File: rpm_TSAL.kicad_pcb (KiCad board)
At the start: 2 copper layers, 0 parts

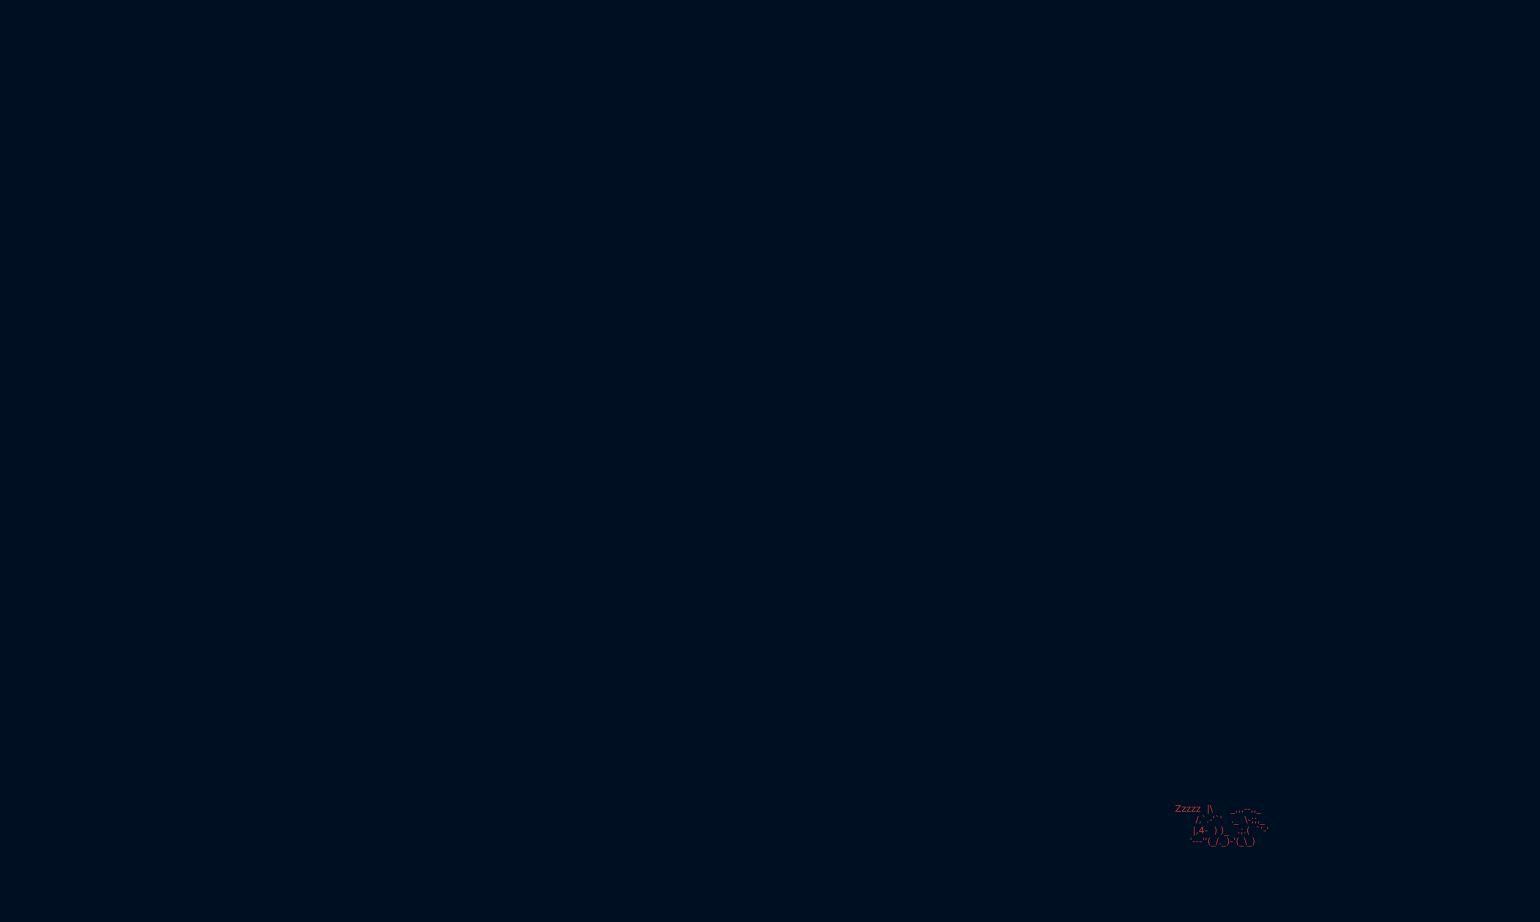
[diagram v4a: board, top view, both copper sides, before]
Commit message: TS Detection routing
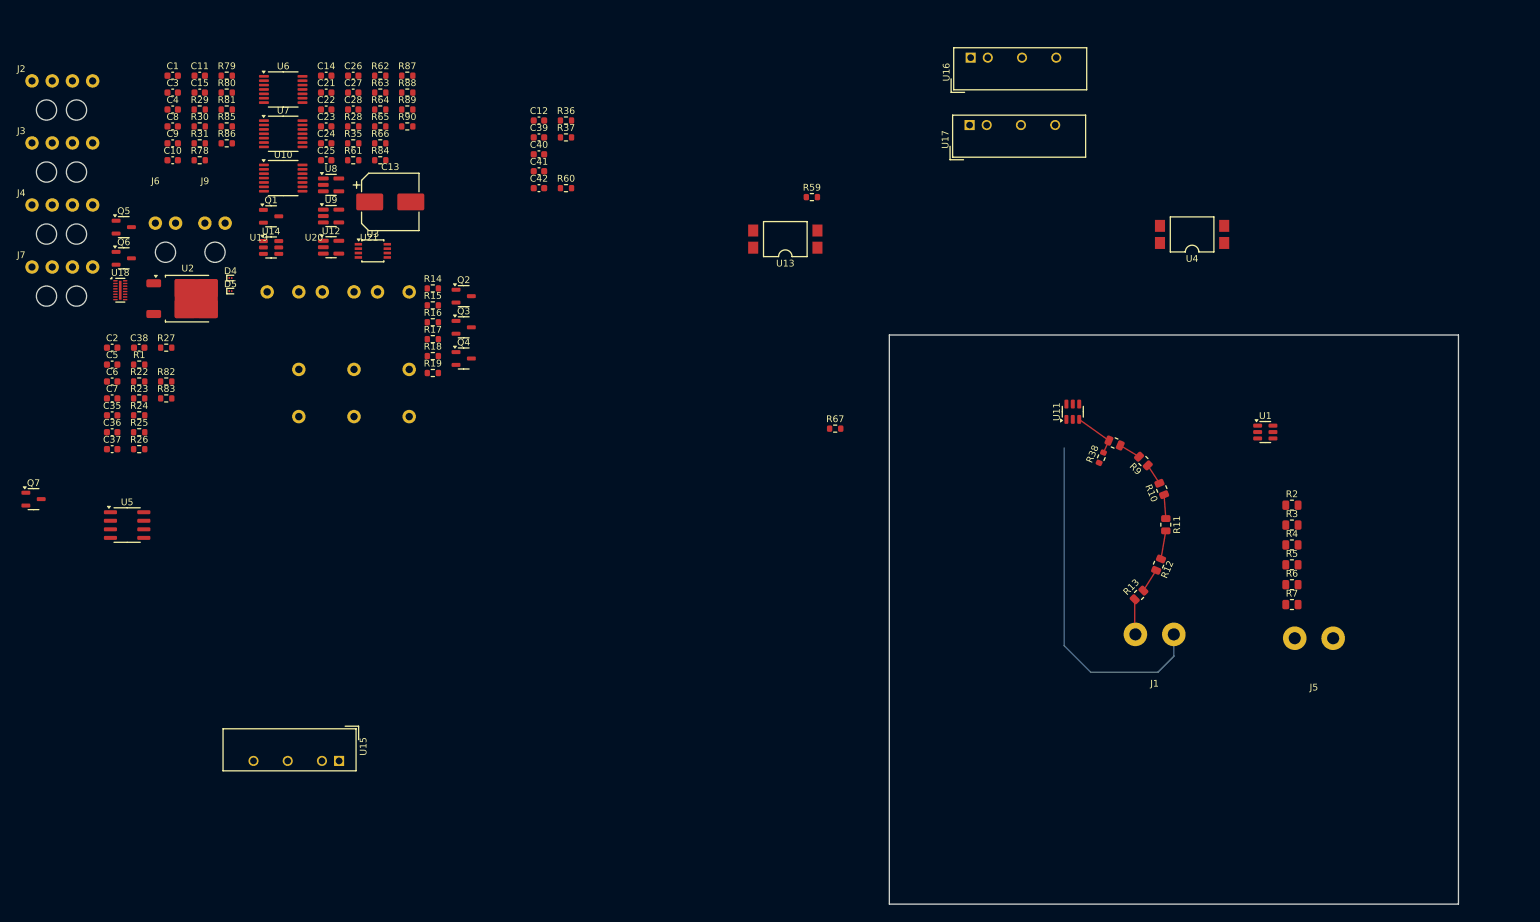
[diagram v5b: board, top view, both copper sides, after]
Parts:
- added C1: 100nF, Capacitor_SMD:C_0603_1608Metric, F.Cu at (45.5, 20.8)
- added C10: 100nF, Capacitor_SMD:C_0603_1608Metric, F.Cu at (45.5, 33.4)
- added C11: 10uF, Capacitor_SMD:C_0603_1608Metric, F.Cu at (49.5, 20.8)
- added C12: 100nF, Capacitor_SMD:C_0603_1608Metric, F.Cu at (99.9, 27.5)
- added C13: C_Polarized, Capacitor_SMD:CP_Elec_8x5.4, F.Cu at (77.8, 39.5)
- added C14: C, Capacitor_SMD:C_0603_1608Metric, F.Cu at (68.3, 20.8)
- added C15: 10uF, Capacitor_SMD:C_0603_1608Metric, F.Cu at (49.5, 23.3)
- added C2: 100nF, Capacitor_SMD:C_0603_1608Metric, F.Cu at (36.5, 61.2)
- added C21: 100nF, Capacitor_SMD:C_0603_1608Metric, F.Cu at (68.3, 23.3)
- added C22: 100nF, Capacitor_SMD:C_0603_1608Metric, F.Cu at (68.3, 25.8)
- added C23: 100nF, Capacitor_SMD:C_0603_1608Metric, F.Cu at (68.3, 28.4)
- added C24: 100nF, Capacitor_SMD:C_0603_1608Metric, F.Cu at (68.3, 30.9)
- added C25: 100nF, Capacitor_SMD:C_0603_1608Metric, F.Cu at (68.3, 33.4)
- added C26: 100nF, Capacitor_SMD:C_0603_1608Metric, F.Cu at (72.3, 20.8)
- added C27: 100nF, Capacitor_SMD:C_0603_1608Metric, F.Cu at (72.3, 23.3)
- added C28: 100nF, Capacitor_SMD:C_0603_1608Metric, F.Cu at (72.3, 25.8)
- added C3: 10uF, Capacitor_SMD:C_0603_1608Metric, F.Cu at (45.5, 23.3)
- added C35: 10uF, Capacitor_SMD:C_0603_1608Metric, F.Cu at (36.5, 71.2)
- added C36: 100nF, Capacitor_SMD:C_0603_1608Metric, F.Cu at (36.5, 73.7)
- added C37: 10uF, Capacitor_SMD:C_0603_1608Metric, F.Cu at (36.5, 76.2)
- added C38: 100nF, Capacitor_SMD:C_0603_1608Metric, F.Cu at (40.5, 61.2)
- added C39: 100nF, Capacitor_SMD:C_0603_1608Metric, F.Cu at (99.9, 30.0)
- added C4: 10uF, Capacitor_SMD:C_0603_1608Metric, F.Cu at (45.5, 25.8)
- added C40: 10uF, Capacitor_SMD:C_0603_1608Metric, F.Cu at (99.9, 32.5)
- added C41: 100nF, Capacitor_SMD:C_0603_1608Metric, F.Cu at (99.9, 35.0)
- added C42: 10uF, Capacitor_SMD:C_0603_1608Metric, F.Cu at (99.9, 37.5)
- added C5: 100nF, Capacitor_SMD:C_0603_1608Metric, F.Cu at (36.5, 63.7)
- added C6: 100nF, Capacitor_SMD:C_0603_1608Metric, F.Cu at (36.5, 66.2)
- added C7: 100nF, Capacitor_SMD:C_0603_1608Metric, F.Cu at (36.5, 68.7)
- added C8: 100nF, Capacitor_SMD:C_0603_1608Metric, F.Cu at (45.5, 28.4)
- added C9: 100nF, Capacitor_SMD:C_0603_1608Metric, F.Cu at (45.5, 30.9)
- added D4: ESD, Diode_SMD:Infineon_SG-WLL-2-3_0.58x0.28_P0.36mm, F.Cu at (54.1, 50.8)
- added D5: ESD, Diode_SMD:Infineon_SG-WLL-2-3_0.58x0.28_P0.36mm, F.Cu at (54.1, 52.8)
- added J1: Conn_01x02, wuerth_conn:657002130101, F.Cu at (188.4, 103.7)
- added J2: Conn_01x04, wuerth_conn:66200411022, F.Cu at (23.0, 20.3)
- added J3: Conn_01x04, wuerth_conn:66200411022, F.Cu at (23.0, 29.5)
- added J4: Conn_01x04, wuerth_conn:66200411022, F.Cu at (23.0, 38.7)
- added J5: Conn_01x02, wuerth_conn:657002130101, F.Cu at (212.0, 104.3)
- added J6: Conn_01x02, wuerth_conn:66200211024, F.Cu at (42.9, 42.7)
- added J7: Conn_01x04, wuerth_conn:66200411022, F.Cu at (23.0, 47.9)
- added J9: Conn_01x02, wuerth_conn:66200211024, F.Cu at (50.3, 42.7)
- added Q1: NMOS, Package_TO_SOT_SMD:SOT-23-3, F.Cu at (60.1, 41.7)
- added Q2: NMOS, Package_TO_SOT_SMD:SOT-23-3, F.Cu at (88.7, 53.5)
- added Q3: NMOS, Package_TO_SOT_SMD:SOT-23-3, F.Cu at (88.7, 58.2)
- added Q4: NMOS, Package_TO_SOT_SMD:SOT-23-3, F.Cu at (88.7, 62.8)
- added Q5: PMOS, Package_TO_SOT_SMD:SOT-23-3, F.Cu at (38.2, 43.3)
- added Q6: PMOS, Package_TO_SOT_SMD:SOT-23-3, F.Cu at (38.2, 47.9)
- added Q7: NMOS, Package_TO_SOT_SMD:SOT-23-3, F.Cu at (24.9, 83.7)
- added R1: 1k, Resistor_SMD:R_0603_1608Metric, F.Cu at (40.5, 63.7)
- added R10: 52k3, Resistor_SMD:R_0805_2012Metric, F.Cu at (192.3, 82.2)
- added R11: 52k3, Resistor_SMD:R_0805_2012Metric, F.Cu at (192.9, 87.5)
- added R12: 52k3, Resistor_SMD:R_0805_2012Metric, F.Cu at (191.8, 93.4)
- added R13: 52k3, Resistor_SMD:R_0805_2012Metric, F.Cu at (188.9, 97.9)
- added R14: 200R, Resistor_SMD:R_0603_1608Metric, F.Cu at (84.1, 52.4)
- added R15: 200R, Resistor_SMD:R_0603_1608Metric, F.Cu at (84.1, 54.9)
- added R16: 200R, Resistor_SMD:R_0603_1608Metric, F.Cu at (84.1, 57.4)
- added R17: 10k, Resistor_SMD:R_0603_1608Metric, F.Cu at (84.1, 59.9)
- added R18: 10k, Resistor_SMD:R_0603_1608Metric, F.Cu at (84.1, 62.4)
- added R19: 10k, Resistor_SMD:R_0603_1608Metric, F.Cu at (84.1, 64.9)
- added R2: 52k3, Resistor_SMD:R_0805_2012Metric, F.Cu at (211.6, 84.5)
- added R22: 1k, Resistor_SMD:R_0603_1608Metric, F.Cu at (40.5, 66.2)
- added R23: 1k, Resistor_SMD:R_0603_1608Metric, F.Cu at (40.5, 68.7)
- added R24: 12k, Resistor_SMD:R_0603_1608Metric, F.Cu at (40.5, 71.2)
- added R25: 1k, Resistor_SMD:R_0603_1608Metric, F.Cu at (40.5, 73.7)
- added R26: 1k, Resistor_SMD:R_0603_1608Metric, F.Cu at (40.5, 76.2)
- added R27: 10k, Resistor_SMD:R_0603_1608Metric, F.Cu at (44.5, 61.2)
- added R28: 30k, Resistor_SMD:R_0603_1608Metric, F.Cu at (72.3, 28.4)
- added R29: 10k, Resistor_SMD:R_0603_1608Metric, F.Cu at (49.5, 25.8)
- added R3: 52k3, Resistor_SMD:R_0805_2012Metric, F.Cu at (211.6, 87.5)
- added R30: 10k, Resistor_SMD:R_0603_1608Metric, F.Cu at (49.5, 28.4)
- added R31: 10k, Resistor_SMD:R_0603_1608Metric, F.Cu at (49.5, 30.9)
- added R35: 200R, Resistor_SMD:R_0603_1608Metric, F.Cu at (72.3, 30.9)
- added R36: 12k, Resistor_SMD:R_0603_1608Metric, F.Cu at (103.9, 27.5)
- added R37: 1k, Resistor_SMD:R_0603_1608Metric, F.Cu at (103.9, 30.0)
- added R38: 1k, Resistor_SMD:R_0603_1608Metric, F.Cu at (183.3, 77.5)
- added R4: 52k3, Resistor_SMD:R_0805_2012Metric, F.Cu at (211.6, 90.5)
- added R5: 52k3, Resistor_SMD:R_0805_2012Metric, F.Cu at (211.6, 93.4)
- added R59: 1k, Resistor_SMD:R_0603_1608Metric, F.Cu at (140.4, 38.8)
- added R6: 52k3, Resistor_SMD:R_0805_2012Metric, F.Cu at (211.6, 96.3)
- added R60: 1k, Resistor_SMD:R_0603_1608Metric, F.Cu at (103.9, 37.5)
- added R61: 10k, Resistor_SMD:R_0603_1608Metric, F.Cu at (72.3, 33.4)
- added R62: 10k, Resistor_SMD:R_0603_1608Metric, F.Cu at (76.3, 20.8)
- added R63: 33k, Resistor_SMD:R_0603_1608Metric, F.Cu at (76.3, 23.3)
- added R64: 33k, Resistor_SMD:R_0603_1608Metric, F.Cu at (76.3, 25.8)
- added R65: 10k, Resistor_SMD:R_0603_1608Metric, F.Cu at (76.3, 28.4)
- added R66: 10k, Resistor_SMD:R_0603_1608Metric, F.Cu at (76.3, 30.9)
- added R67: 1k, Resistor_SMD:R_0603_1608Metric, F.Cu at (143.8, 73.2)
- added R7: 52k3, Resistor_SMD:R_0805_2012Metric, F.Cu at (211.6, 99.3)
- added R78: 200R, Resistor_SMD:R_0603_1608Metric, F.Cu at (49.5, 33.4)
- added R79: 200R, Resistor_SMD:R_0603_1608Metric, F.Cu at (53.5, 20.8)
- added R8: 52k3, Resistor_SMD:R_0805_2012Metric, F.Cu at (185.3, 75.3)
- added R80: 10k, Resistor_SMD:R_0603_1608Metric, F.Cu at (53.5, 23.3)
- added R81: 10k, Resistor_SMD:R_0603_1608Metric, F.Cu at (53.5, 25.8)
- added R82: 200R, Resistor_SMD:R_0603_1608Metric, F.Cu at (44.5, 66.2)
- added R83: 10k, Resistor_SMD:R_0603_1608Metric, F.Cu at (44.5, 68.7)
- added R84: 30k, Resistor_SMD:R_0603_1608Metric, F.Cu at (76.3, 33.4)
- added R85: 30k, Resistor_SMD:R_0603_1608Metric, F.Cu at (53.5, 28.4)
- added R86: 7k5, Resistor_SMD:R_0603_1608Metric, F.Cu at (53.5, 30.9)
- added R87: 30k, Resistor_SMD:R_0603_1608Metric, F.Cu at (80.3, 20.8)
- added R88: 7k5, Resistor_SMD:R_0603_1608Metric, F.Cu at (80.3, 23.3)
- added R89: 7k5, Resistor_SMD:R_0603_1608Metric, F.Cu at (80.3, 25.8)
- added R9: 52k3, Resistor_SMD:R_0805_2012Metric, F.Cu at (189.6, 78.0)
- added R90: 7k5, Resistor_SMD:R_0603_1608Metric, F.Cu at (80.3, 28.4)
- added U1: OPA355NA, Package_TO_SOT_SMD:SOT-23-6, F.Cu at (207.6, 73.7)
- added U10: SN74HCS266PWR, Package_SO:TSSOP-14_4.4x5mm_P0.65mm, F.Cu at (61.9, 36.0)
- added U11: OPA355NA, Package_TO_SOT_SMD:SOT-23-6, F.Cu at (179.1, 70.7)
- added U12: 74LVC1G32GV, Package_SO:SC-74A-5_1.55x2.9mm_P0.95mm, F.Cu at (69.0, 46.3)
- added U13: SFH617A-1X007T, Package_DIP:SMDIP-4_W9.53mm_Clearance8mm, F.Cu at (136.4, 45.1)
- added U14: OPA355NA, Package_TO_SOT_SMD:SOT-23-6, F.Cu at (60.1, 46.3)
- added U15: TBA1-1211E, Converter_DCDC:Converter_DCDC_TRACO_TBA1-xxxxE_Single_THT, F.Cu at (70.2, 122.5)
- added U16: TBA1-0511E, Converter_DCDC:Converter_DCDC_TRACO_TBA1-xxxxE_Single_THT, F.Cu at (163.9, 18.1)
- added U17: TBA1-0511E, Converter_DCDC:Converter_DCDC_TRACO_TBA1-xxxxE_Single_THT, F.Cu at (163.8, 28.1)
- added U18: IP4252CZ16, Package_SON:Nexperia_HUSON-16_USON-16-1EP_1.35x3.3mm_P0.4mm_EP0.4x2.8mm, F.Cu at (37.7, 52.7)
- added U19: ~, Zettler:AZ9371, F.Cu at (58.3, 51.9)
- added U2: L7805, Package_TO_SOT_SMD:TO-252-2, F.Cu at (47.7, 53.9)
- added U20: ~, Zettler:AZ9371, F.Cu at (66.5, 51.9)
- added U21: ~, Zettler:AZ9371, F.Cu at (74.7, 51.9)
- added U3: 74LVC2G74, Package_SO:TSSOP-8_3x3mm_P0.65mm, F.Cu at (75.2, 46.8)
- added U4: SFH617A-1X007T, Package_DIP:SMDIP-4_W9.53mm_Clearance8mm, F.Cu at (196.8, 44.4)
- added U5: NE555D, Package_SO:SOIC-8_3.9x4.9mm_P1.27mm, F.Cu at (38.8, 87.5)
- added U6: CD74HC30PWR, Package_SO:TSSOP-14_4.4x5mm_P0.65mm, F.Cu at (61.9, 22.9)
- added U7: 4072, Package_SO:TSSOP-14_4.4x5mm_P0.65mm, F.Cu at (61.9, 29.4)
- added U8: 4001, Package_SO:SC-74A-5_1.55x2.9mm_P0.95mm, F.Cu at (69.0, 37.0)
- added U9: 74LVC1G32GV, Package_SO:SC-74A-5_1.55x2.9mm_P0.95mm, F.Cu at (69.0, 41.6)
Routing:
- net HV-: track 0.00 -> 51.5 mm
- net Net-(U11-+): track 0.00 -> 7.37 mm
- net  HV+: track 0.00 -> 5.25 mm
- net Net-(R11-Pad2): track 0.00 -> 4.23 mm
- net Net-(R12-Pad2): track 0.00 -> 3.56 mm
- net Net-(R10-Pad1): track 0.00 -> 3.55 mm
- net Net-(R8-Pad1): track 0.00 -> 3.25 mm
- net Net-(R10-Pad2): track 0.00 -> 3.18 mm
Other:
- board outline added: 84.5 x 84.5 mm
- board text removed: "Zzzzz |\ _,,,--,,_ /,`.-'`' ._ \-;;,_ |,4- ) )_ .;.( `'-' '---''(_/._)-'(_\_)"

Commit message: Misc.
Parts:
- moved U1 5.88 mm to (206.4, 68.0)
- moved U11 2.28 mm to (179.0, 73.0)
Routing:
- net Net-(U11-+): track 7.37 -> 6.50 mm
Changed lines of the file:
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@@
 		(tags "SMD DIP DIL PDIP SMDIP 2.54mm 9.53mm 375mil Clearance8mm")
 		(property "Reference" "U4"
-			(at 0 -3.6 360)
+			(at 0 -3.6 0)
 			(layer "F.SilkS")
 			(effects
@@
 		)
 		(property "Value" "SFH617A-1X007T"
-			(at -0.15 4.12 360)
+			(at -0.15 4.12 0)
 			(layer "F.Fab")
 			(effects
@@
 		)
 		(fp_text user "${REFERENCE}"
-			(at 0 0 360)
+			(at 0 0 0)
 			(layer "F.Fab")
 			(effects
@@
 		(tags "resistor")
 		(property "Reference" "R38"
-			(at 0 -1.43 67)
+			(at 0.030294 -1.808229 67)
 			(layer "F.SilkS")
 			(effects
@@
 	(footprint "Package_TO_SOT_SMD:SOT-23-6"
 		(layer "F.Cu")
-		(at 179.075 70.6875 90)
+		(at 179.025 72.9625 90)
 		(descr "SOT, 6 Pin (https://www.jedec.org/sites/default/files/docs/Mo-178c.PDF variant AB), generated with kicad-footprint-generator ipc_gullwing_generator.py")
 		(tags "SOT TO_SOT_SMD")
@@
 		(tags "SMD DIP DIL PDIP SMDIP 2.54mm 9.53mm 375mil Clearance8mm")
 		(property "Reference" "U13"
-			(at 0 -3.6 360)
+			(at 0 -3.6 0)
 			(layer "F.SilkS")
 			(effects
@@
 		)
 		(property "Value" "SFH617A-1X007T"
-			(at 0 3.6 360)
+			(at 0 3.6 0)
 			(layer "F.Fab")
 			(effects
@@
 		)
 		(fp_text user "${REFERENCE}"
-			(at 0 0 360)
+			(at 0 0 0)
 			(layer "F.Fab")
 			(effects
@@
 		(tags "resistor")
 		(property "Reference" "R8"
-			(at 0 -1.65 157)
+			(at 0.03661 1.749796 157)
 			(layer "F.SilkS")
-			(hide yes)
 			(effects
 				(font
@@
 	(footprint "Package_TO_SOT_SMD:SOT-23-6"
 		(layer "F.Cu")
-		(at 207.6375 73.7)
+		(at 206.3875 67.95)
 		(descr "SOT, 6 Pin (https://www.jedec.org/sites/default/files/docs/Mo-178c.PDF variant AB), generated with kicad-footprint-generator ipc_gullwing_generator.py")
 		(tags "SOT TO_SOT_SMD")
 		(property "Reference" "U1"
-			(at 0 -2.4 360)
+			(at 0 -2.4 0)
 			(layer "F.SilkS")
 			(effects
@@
 		)
 		(property "Value" "OPA355NA"
-			(at -0.55 2.4 360)
+			(at -0.55 2.4 0)
 			(layer "F.Fab")
 			(effects
@@
 		)
 		(fp_text user "${REFERENCE}"
-			(at 0 0 360)
+			(at 0 0 0)
 			(layer "F.Fab")
 			(effects
@@
 	)
 	(segment
-		(start 184.435039 74.968458)
-		(end 180.025 71.825)
+		(start 179.975 74.1)
+		(end 184.435039 74.968458)
 		(width 0.2)
 		(layer "F.Cu")

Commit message: TSAL Rev 0.2
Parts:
- removed J9: Conn_01x02, wuerth_conn:66200211024
- added J14: Conn_01x04, wuerth_conn:66200411022, F.Cu at (129.2, 103.0)
- R85: value 30k -> 30k
- R86, R88, R89, R90: value 7k5 -> e
- moved C5 168.5 mm to (205.0, 69.4), turned to -90 degrees
- moved R23 162.5 mm to (203.1, 72.2), turned to 90 degrees
- moved R24 160.7 mm to (201.2, 69.2), turned to 180 degrees
- moved R22 160.0 mm to (200.3, 75.7)
- moved C35 148.5 mm to (182.9, 46.1), turned to -90 degrees
- moved C36 147.3 mm to (181.2, 46.1), turned to -90 degrees
- moved R1 121.6 mm to (162.0, 57.6)
- moved C12 87.0 mm to (177.3, 67.0)
- moved R37 85.7 mm to (179.2, 70.9), turned to 90 degrees
- moved R36 84.2 mm to (176.7, 69.8), turned to 180 degrees
- moved R60 64.5 mm to (162.0, 65.5)
- moved R59 45.6 mm to (177.4, 65.5), turned to 180 degrees
- moved U13 37.9 mm to (167.4, 67.0)
- moved R67 36.6 mm to (177.0, 57.8), turned to 180 degrees
- moved U16 33.1 mm to (162.6, 51.2)
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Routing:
- net HV_RED-: track 0.00 -> 109.1 mm, vias 0 -> 3
- net +5V_{iso_RED}: track 0.00 -> 47.2 mm
- net Net-(U1-Pad1): track 0.00 -> 32.5 mm
- net +5V_{iso}: track 0.00 -> 22.4 mm, vias 0 -> 1
- net HV-: track 51.5 -> 66.6 mm, vias 0 -> 1
- net Net-(U11-Pad1): track 0.00 -> 6.96 mm
- net Net-(U1-+): track 0.00 -> 6.15 mm
- net  HV_RED+: track 0.00 -> 5.62 mm
- net Net-(R59-Pad2): track 0.00 -> 4.50 mm
- net Net-(U1--): track 0.00 -> 4.34 mm
- net Net-(R11-Pad2): track 4.23 -> 0.00 mm
- net Net-(R67-Pad2): track 0.00 -> 4.08 mm
- net Net-(R12-Pad2): track 3.56 -> 0.00 mm
- net Net-(R10-Pad1): track 3.55 -> 0.00 mm
- net Net-(U11--): track 0.00 -> 3.49 mm
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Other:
- board size 84.5 x 84.5 mm -> 71.6 x 69.5 mm
- copper layers 2 -> 4

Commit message: Added Seperate Project
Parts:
- removed D4: ESD, Diode_SMD:Infineon_SG-WLL-2-3_0.58x0.28_P0.36mm
- removed J5: Conn_01x02, wuerth_conn:657002130101
- removed Q6: PMOS, Package_TO_SOT_SMD:SOT-23-3
- removed R79: 200R, Resistor_SMD:R_0603_1608Metric
- removed R80: 10k, Resistor_SMD:R_0603_1608Metric
- added H1: MountingHole, MountingHole:MountingHole_3.2mm_M3_DIN965, F.Cu at (66.3, 21.2)
- added H2: MountingHole, MountingHole:MountingHole_3.2mm_M3_DIN965, F.Cu at (66.3, 28.3)
- added H3: MountingHole, MountingHole:MountingHole_3.2mm_M3_DIN965, F.Cu at (66.3, 35.5)
- added H4: MountingHole, MountingHole:MountingHole_3.2mm_M3_DIN965, F.Cu at (66.3, 42.6)
- J7: value Conn_01x04 -> Conn_01x02; footprint wuerth_conn:66200411022 -> wuerth_conn:66200211024
- moved R7 145.9 mm to (79.9, 33.8), turned to 0 degrees
- moved R6 143.9 mm to (79.9, 30.9), turned to 0 degrees
- moved R5 142.0 mm to (79.9, 27.9), turned to 0 degrees
- moved R4 140.0 mm to (79.9, 25.0), turned to 0 degrees
- moved R3 138.1 mm to (79.9, 22.0), turned to 0 degrees
- moved R2 136.1 mm to (79.9, 19.1), turned to 0 degrees
- moved U1 130.5 mm to (72.4, 46.0), turned to 0 degrees
- moved C5 130.1 mm to (84.1, 21.4), turned to 0 degrees
- moved R13 124.8 mm to (62.9, 96.4), turned to 0 degrees
- moved R23 123.7 mm to (88.1, 26.4), turned to 0 degrees
- moved R22 123.5 mm to (88.1, 23.9)
- moved R12 122.8 mm to (62.9, 93.5), turned to 0 degrees
- moved R11 120.8 mm to (62.9, 90.5), turned to 0 degrees
- moved R24 120.1 mm to (88.1, 28.9), turned to 0 degrees
- moved R10 118.8 mm to (62.9, 87.6), turned to 0 degrees
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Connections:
- net  HV+ renamed HV+
- net /LV Connectors/TSAL_LED_RED renamed /TSAL RED/TSAL_RED_OUT
- J7 pad 2: Net-(D4-A2) -> GND
- Q5 pad 1: +24V -> Net-(D5-A2)
- Q5 pad 3: Net-(D5-A2) -> +24V
- R7 pad 1:  HV_RED+ -> HV_RED+
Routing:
- net HV_RED-: track 109.1 -> 0.00 mm, vias 3 -> 0
- net HV-: track 66.6 -> 0.00 mm, vias 1 -> 0
- net +5V_{iso_RED}: track 47.2 -> 0.00 mm
- net Net-(U1-Pad1): track 32.5 -> 0.00 mm
- net +5V_{iso}: track 22.4 -> 0.00 mm, vias 1 -> 0
- net Net-(U11-Pad1): track 6.96 -> 0.00 mm
- net Net-(U1-+): track 6.15 -> 0.00 mm
- net  HV_RED+: track 5.62 -> 0.00 mm
- net HV+: track 5.40 -> 0.00 mm
- net Net-(R59-Pad2): track 4.50 -> 0.00 mm
- net Net-(U11-+): track 4.41 -> 0.00 mm
- net Net-(U1--): track 4.34 -> 0.00 mm
- net Net-(R67-Pad2): track 4.08 -> 0.00 mm
- net Net-(U11--): track 3.49 -> 0.00 mm
- net Net-(R6-Pad2): track 2.65 -> 0.00 mm
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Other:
- board outline removed
